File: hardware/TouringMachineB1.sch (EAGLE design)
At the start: 64 parts, among them IC1 78L05F, J1 PJ301_THONKICONN6, J2 PJ301_THONKICONN6, J3 PJ301_THONKICONN6, J4 PJ301_THONKICONN6, J5 POWER_SIMPLE10-OTHERSIDE, U1 MCP6002_, U2 TL072_SMD

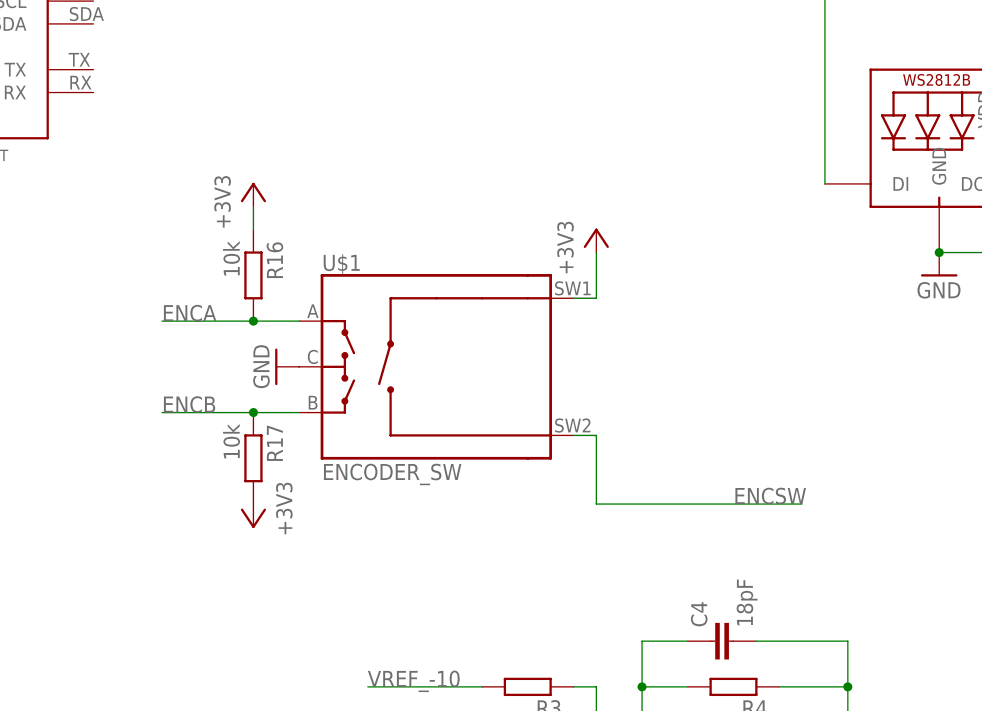
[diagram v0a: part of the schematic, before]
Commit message: cleaned up UI after knobtesterA results
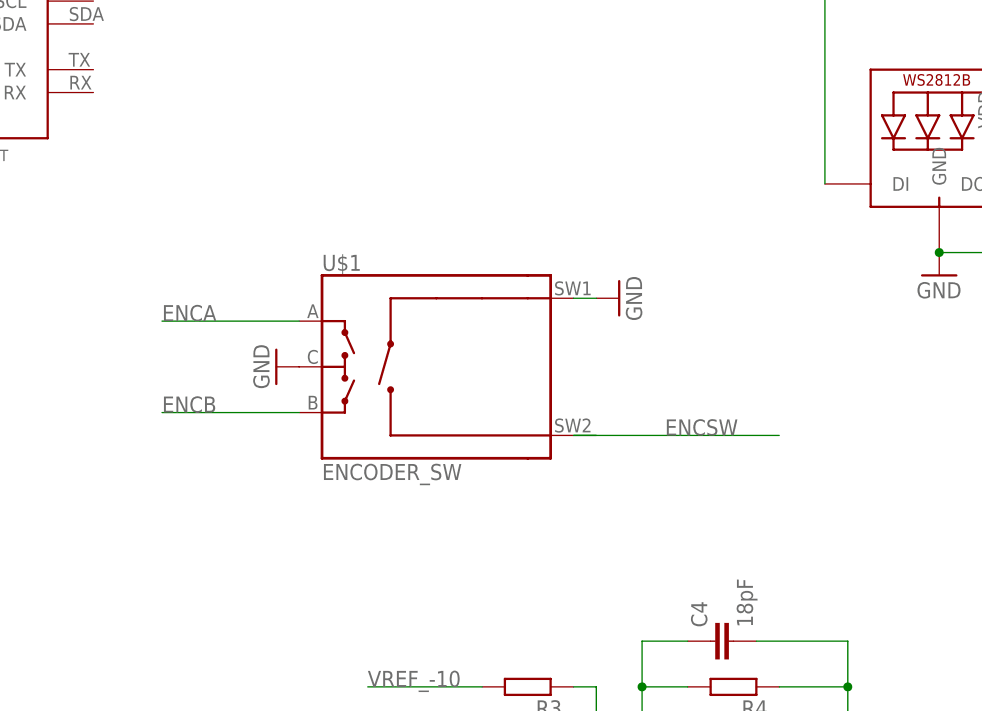
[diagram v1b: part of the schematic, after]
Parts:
- removed R16, R17: 10k, resistor:R-EU_R0603
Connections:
- net +3V3: no longer R16.1, R17.2, U$1.SW1
- net ENCA: no longer R16.2
- net ENCB: no longer R17.1
- net GND: now also U$1.SW1
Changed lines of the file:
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@@
 <part name="GND28" library="supply1" library_urn="urn:adsk.eagle:library:371" deviceset="GND" device=""/>
 <part name="GND29" library="supply1" library_urn="urn:adsk.eagle:library:371" deviceset="GND" device=""/>
-<part name="+3V6" library="supply1" library_urn="urn:adsk.eagle:library:371" deviceset="+3V3" device=""/>
-<part name="R16" library="resistor" library_urn="urn:adsk.eagle:library:348" deviceset="R-EU_" device="R0603" package3d_urn="urn:adsk.eagle:package:23555/3" value="10k"/>
-<part name="R17" library="resistor" library_urn="urn:adsk.eagle:library:348" deviceset="R-EU_" device="R0603" package3d_urn="urn:adsk.eagle:package:23555/3" value="10k"/>
-<part name="+3V7" library="supply1" library_urn="urn:adsk.eagle:library:371" deviceset="+3V3" device=""/>
-<part name="+3V8" library="supply1" library_urn="urn:adsk.eagle:library:371" deviceset="+3V3" device=""/>
 <part name="U$1" library="halcyonmod_Switches" deviceset="ENCODER_SW" device="" override_package3d_urn="urn:adsk.eagle:package:22891623/2" override_package_urn="urn:adsk.eagle:footprint:22891624/1"/>
 <part name="C9" library="resistor" library_urn="urn:adsk.eagle:library:348" deviceset="C-EU" device="C0603" package3d_urn="urn:adsk.eagle:package:23616/2" value="100n"/>
@@
 <part name="GND19" library="supply1" library_urn="urn:adsk.eagle:library:371" deviceset="GND" device=""/>
 <part name="GND30" library="supply1" library_urn="urn:adsk.eagle:library:371" deviceset="GND" device=""/>
+<part name="GND31" library="supply1" library_urn="urn:adsk.eagle:library:371" deviceset="GND" device=""/>
 </parts>
 <sheets>
@@
 <attribute name="VALUE" x="81.28" y="129.54" size="1.778" layer="96" rot="R270"/>
 </instance>
-<instance part="+3V6" gate="G$1" x="81.28" y="147.32" smashed="yes">
-<attribute name="VALUE" x="78.74" y="142.24" size="1.778" layer="96" rot="R90"/>
-</instance>
-<instance part="R16" gate="G$1" x="81.28" y="137.16" smashed="yes" rot="R270">
-<attribute name="NAME" x="82.7786" y="140.97" size="1.778" layer="95" rot="R270"/>
-<attribute name="VALUE" x="77.978" y="140.97" size="1.778" layer="96" rot="R270"/>
-</instance>
-<instance part="R17" gate="G$1" x="81.28" y="116.84" smashed="yes" rot="R270">
-<attribute name="NAME" x="82.7786" y="120.65" size="1.778" layer="95" rot="R270"/>
-<attribute name="VALUE" x="77.978" y="120.65" size="1.778" layer="96" rot="R270"/>
-</instance>
-<instance part="+3V7" gate="G$1" x="81.28" y="109.22" smashed="yes" rot="R180">
-<attribute name="VALUE" x="83.82" y="114.3" size="1.778" layer="96" rot="R270"/>
-</instance>
-<instance part="+3V8" gate="G$1" x="119.38" y="142.24" smashed="yes">
-<attribute name="VALUE" x="116.84" y="137.16" size="1.778" layer="96" rot="R90"/>
-</instance>
 <instance part="U$1" gate="G$1" x="101.6" y="127" smashed="yes">
 <attribute name="NAME" x="88.9" y="137.668" size="1.778" layer="95"/>
@@
 <instance part="GND30" gate="1" x="248.92" y="40.64" smashed="yes" rot="MR270">
 <attribute name="VALUE" x="251.46" y="43.18" size="1.778" layer="96" rot="MR270"/>
+</instance>
+<instance part="GND31" gate="1" x="121.92" y="134.62" smashed="yes" rot="R90">
+<attribute name="VALUE" x="124.46" y="132.08" size="1.778" layer="96" rot="R90"/>
 </instance>
 </instances>
@@
 <pinref part="C10" gate="G$1" pin="1"/>
 <pinref part="GND30" gate="1" pin="GND"/>
+</segment>
+<segment>
+<pinref part="U$1" gate="G$1" pin="SW1"/>
+<wire x1="119.38" y1="134.62" x2="116.84" y2="134.62" width="0.1524" layer="91"/>
+<pinref part="GND31" gate="1" pin="GND"/>
 </segment>
 </net>
@@
 <wire x1="180.34" y1="71.12" x2="180.34" y2="68.58" width="0.1524" layer="91"/>
 </segment>
-<segment>
-<pinref part="R16" gate="G$1" pin="1"/>
-<pinref part="+3V6" gate="G$1" pin="+3V3"/>
-<wire x1="81.28" y1="144.78" x2="81.28" y2="142.24" width="0.1524" layer="91"/>
-</segment>
-<segment>
-<pinref part="R17" gate="G$1" pin="2"/>
-<pinref part="+3V7" gate="G$1" pin="+3V3"/>
-</segment>
-<segment>
-<pinref part="+3V8" gate="G$1" pin="+3V3"/>
-<wire x1="119.38" y1="139.7" x2="119.38" y2="134.62" width="0.1524" layer="91"/>
-<pinref part="U$1" gate="G$1" pin="SW1"/>
-<wire x1="119.38" y1="134.62" x2="116.84" y2="134.62" width="0.1524" layer="91"/>
-</segment>
 </net>
 <net name="KNOB2" class="0">
@@
 <net name="ENCA" class="0">
 <segment>
-<wire x1="86.36" y1="132.08" x2="81.28" y2="132.08" width="0.1524" layer="91"/>
-<pinref part="R16" gate="G$1" pin="2"/>
-<wire x1="81.28" y1="132.08" x2="71.12" y2="132.08" width="0.1524" layer="91"/>
-<junction x="81.28" y="132.08"/>
+<wire x1="86.36" y1="132.08" x2="71.12" y2="132.08" width="0.1524" layer="91"/>
 <label x="71.12" y="132.08" size="1.778" layer="95"/>
 <pinref part="U$1" gate="G$1" pin="A"/>
@@
 <net name="ENCB" class="0">
 <segment>
-<wire x1="86.36" y1="121.92" x2="81.28" y2="121.92" width="0.1524" layer="91"/>
-<pinref part="R17" gate="G$1" pin="1"/>
-<wire x1="81.28" y1="121.92" x2="71.12" y2="121.92" width="0.1524" layer="91"/>
-<junction x="81.28" y="121.92"/>
+<wire x1="86.36" y1="121.92" x2="71.12" y2="121.92" width="0.1524" layer="91"/>
 <label x="71.12" y="121.92" size="1.778" layer="95"/>
 <pinref part="U$1" gate="G$1" pin="B"/>
@@
 <net name="ENCSW" class="0">
 <segment>
-<wire x1="116.84" y1="119.38" x2="119.38" y2="119.38" width="0.1524" layer="91"/>
-<wire x1="119.38" y1="119.38" x2="119.38" y2="111.76" width="0.1524" layer="91"/>
-<wire x1="119.38" y1="111.76" x2="142.24" y2="111.76" width="0.1524" layer="91"/>
-<label x="134.62" y="111.76" size="1.778" layer="95"/>
+<wire x1="119.38" y1="119.38" x2="116.84" y2="119.38" width="0.1524" layer="91"/>
+<wire x1="116.84" y1="119.38" x2="139.7" y2="119.38" width="0.1524" layer="91"/>
+<label x="127" y="119.38" size="1.778" layer="95"/>
 <pinref part="U$1" gate="G$1" pin="SW2"/>
 </segment>
